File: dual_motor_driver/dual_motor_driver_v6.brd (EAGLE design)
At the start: 80 x 40 mm, 86 parts, among them IC1 MCP602SN

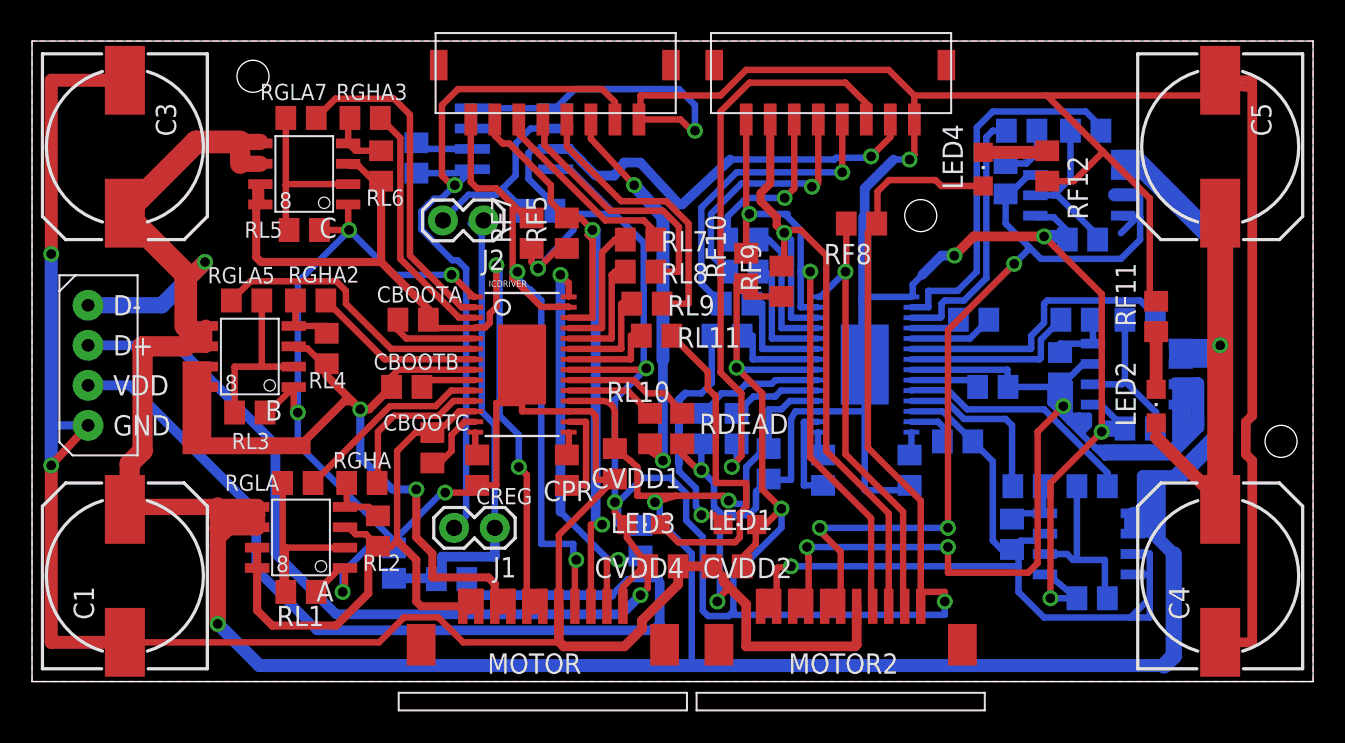
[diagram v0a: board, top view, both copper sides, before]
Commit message: fixed tension sensor amplifier
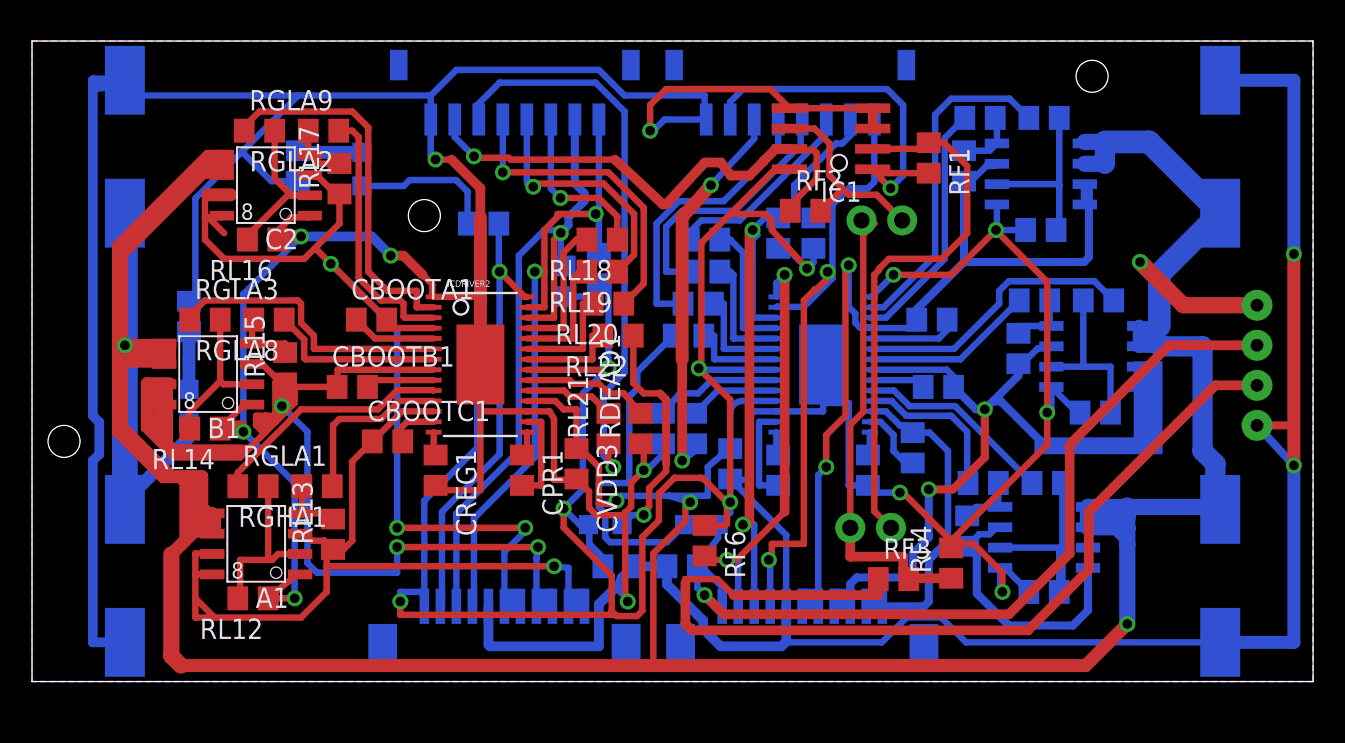
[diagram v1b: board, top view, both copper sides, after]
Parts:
- moved U$3 73.0 mm to (76.5, 16.0), flipped to the bottom
- moved C1 68.4 mm to (74.2, 6.60), flipped to the bottom
- moved C3 68.4 mm to (74.2, 33.4), flipped to the bottom
- moved C4 68.4 mm to (5.80, 6.60), flipped to the bottom
- moved C5 68.4 mm to (5.80, 33.4), flipped to the bottom
- moved LED2 60.4 mm to (9.80, 17.2), flipped to the bottom
- moved RF11 60.4 mm to (9.80, 22.8), flipped to the bottom
- moved RGLA3 58.4 mm to (10.8, 22.6), flipped to the top
- moved RL14 58.4 mm to (10.8, 15.8), flipped to the top
- moved B1 58.0 mm to (11.0, 19.2), flipped to the top
- moved RGLA5 53.2 mm to (66.6, 23.8), flipped to the bottom
- moved B 52.8 mm to (66.4, 20.3), flipped to the bottom
- moved RL3 52.8 mm to (66.4, 16.8), flipped to the bottom
- moved RGLA1 52.4 mm to (13.8, 12.2), flipped to the top
- moved RL12 52.4 mm to (13.8, 5.20), flipped to the top
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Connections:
- removed net N$76: IC1.2, RF1.1
- new net N$52: IC1.2, J1.2, RF1.1
- net VOUT1: no longer J1.2
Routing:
- net N$52: track 0.00 -> 34.5 mm
- net VOUT1: track 47.7 -> 23.2 mm
- net N$76: track 3.66 -> 0.00 mm
